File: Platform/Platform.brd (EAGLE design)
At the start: 34 x 34.3 mm, 21 parts, among them IC1 5v

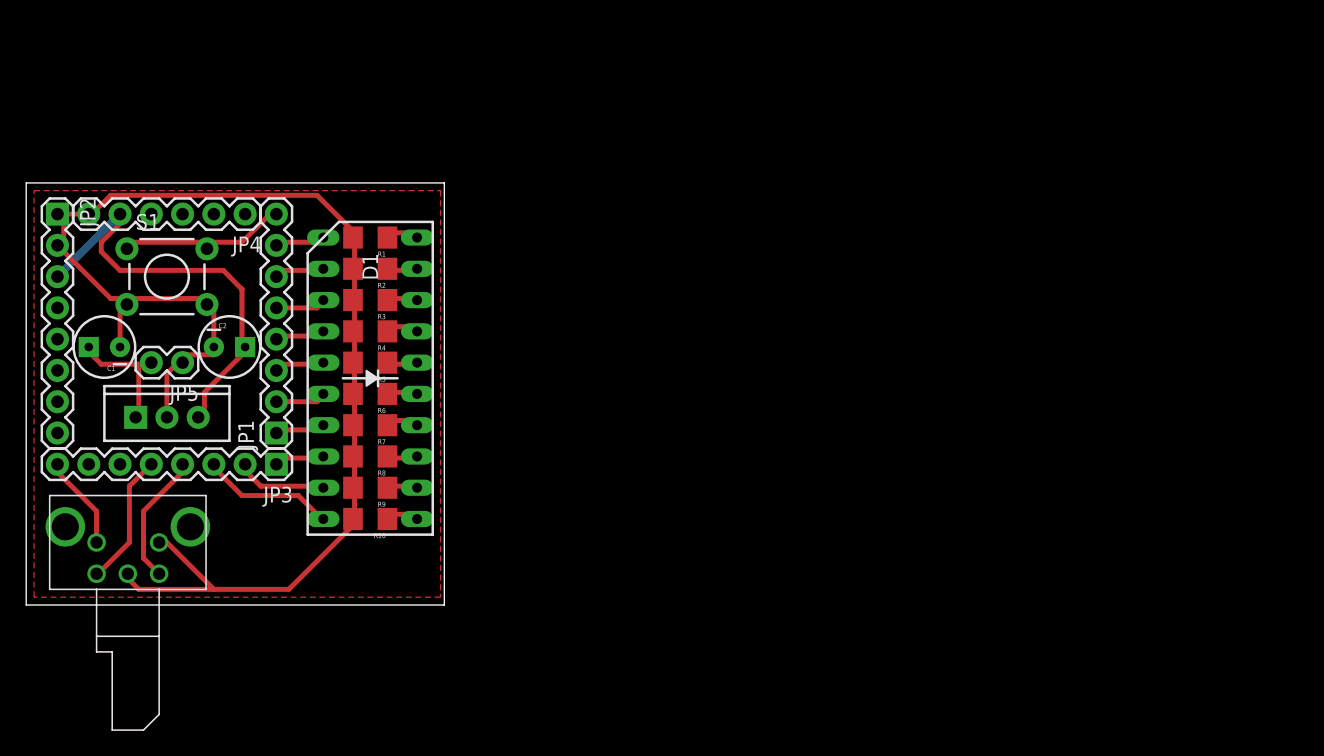
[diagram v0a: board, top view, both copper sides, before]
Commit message: fixed up design rules. Copied the actual newest boards into t the project
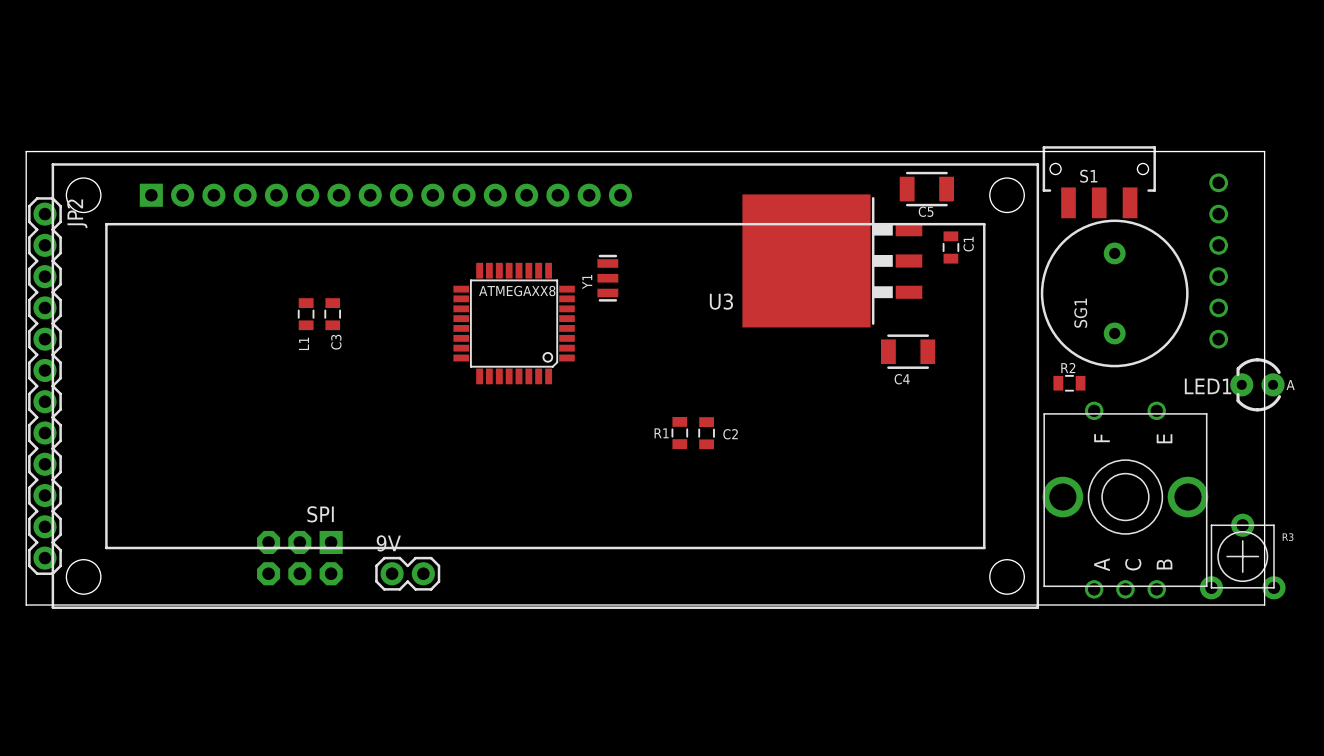
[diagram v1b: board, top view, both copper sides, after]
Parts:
- removed D1: (no value), SparkFun:LED_BARGAPH_10
- removed IC1: 5v, SparkFun:TO220-IGO
- removed JP3: (no value), SparkFun:1X08
- removed JP4: (no value), SparkFun:1X06
- removed JP5: power, SparkFun:1X02
- removed R10, R4, R5, R6, R7, R8, R9: (no value), SparkFun:1206
- removed U$1: EN12-VS11AF, Dustin:12MM_ROTARY
- added 9V: (no value), SparkFun:1X02
- added ATMEGAXX8: ATMEGA168, SparkFun:TQFP32-08
- added C3: 0.1uF, SparkFun:0805
- added C4, C5: 22uf, SparkFun:1210
- added L1: 10uH, SparkFun:0805
- added LED1: (no value), SparkFun:LED3MM
- added SG1: BUZZERPTH, SparkFun:BUZZER-12MM
- added SPI: AVR_SPI_PRG_6NS, SparkFun:2X3-NS
- added U$2: EN12-VS11AFTOPKNOB, Dustin:12MM_ROTATY_TOP
- added U1: LCD-16X2SILK, SparkFun:LCD-16X2
- added U3: IFX25001TC, Dustin:TO263-3
- added Y1: RESONATORSMD, SparkFun:RESONATOR-SMD
- C1, C2: value 22uf -> 0.1uF; device SparkFun:CPOL-RADIAL-10UF-25V -> SparkFun:0805
- JP1: value (none) -> FTDI Basic; device SparkFun:1X08 -> SparkFun:1X06
- JP2: value (none) -> M12PTH; device SparkFun:1X08 -> SparkFun:1X12
- R1: value (none) -> 10K; device SparkFun:1206 -> SparkFun:0805
- R2: value (none) -> 220; device SparkFun:1206 -> SparkFun:0805
- R3: value (none) -> 10k; device SparkFun:1206 -> SparkFun:TRIM_POT_PTH
- S1: value Reset -> (none); device SparkFun:TACTILE-PTH -> SparkFun:SWITCH-SPDT-SMD
- moved JP1 79.2 mm to (96.9, 34.3), turned to 270 degrees
- moved S1 76.2 mm to (87.2, 35.4)
- moved R3 73.9 mm to (98.8, 3.94), turned to 0 degrees
- moved C1 69.2 mm to (75.1, 29.0), turned to 90 degrees
- moved R2 57.6 mm to (84.7, 18.0), turned to 0 degrees
- moved C2 39.4 mm to (55.3, 14.0), turned to 90 degrees
- moved R1 29.7 mm to (53.1, 14.0), turned to 270 degrees
- moved JP2 1.02 mm to (1.52, 31.8)
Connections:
- removed net D11: D1.3, JP1.5
- removed net D12: D1.2, JP1.6
- removed net D13: D1.1, JP1.7
- removed net N$10: D1.20, R1.1
- removed net N$11: D1.19, R2.1
- removed net N$12: D1.18, R3.1
- removed net N$13: D1.17, R4.1
- removed net N$14: D1.16, R5.1
- removed net N$15: D1.15, R6.1
- removed net N$16: D1.14, R7.1
- removed net N$17: D1.13, R8.1
- removed net N$18: D1.12, R9.1
- removed net N$19: D1.11, R10.1
- removed net RST: JP1.8, S1.1, S1.2
- new net AVCC: ATMEGAXX8.18, C3.2, L1.1
- new net CONTRAST: R3.2, U1.3
- new net D11/MOSI: ATMEGAXX8.15, SPI.4
- new net D12/MISO: ATMEGAXX8.16, SPI.1, U$2.E
- new net D13/SCK: ATMEGAXX8.17, LED1.A, SPI.3
- new net N$2: LED1.K, R2.2
- new net RAW_IN: 9V.1, S1.2
- new net RESET: ATMEGAXX8.29, C2.2, R1.1, SPI.5
- new net XTAL1: ATMEGAXX8.7, Y1.1
- new net XTAL2: ATMEGAXX8.8, Y1.3
- net A0: now also ATMEGAXX8.23, U$2.A; no longer JP2.4
- net A1: now also ATMEGAXX8.24, JP2.3; no longer JP2.5
- net A2: now also ATMEGAXX8.25, JP2.4; no longer JP2.6
- net A3: now also ATMEGAXX8.26, JP2.5; no longer JP2.7
- net A4: now also ATMEGAXX8.27, JP2.6; no longer JP2.8
- net A5: now also ATMEGAXX8.28, JP2.7; no longer JP3.8, U$1.D
- net A6: now also ATMEGAXX8.19, JP2.8; no longer JP3.7
- net A7: now also ATMEGAXX8.22, JP2.9; no longer JP3.6
- net AREF: now also ATMEGAXX8.20; no longer JP4.1
- net D10: now also ATMEGAXX8.14, U1.4; no longer D1.4, JP1.4
- net D2: now also ATMEGAXX8.32, U$2.B; no longer JP3.5, U$1.A
- net D3: now also ATMEGAXX8.1, JP2.12; no longer JP3.4, U$1.B
- net D4: now also ATMEGAXX8.2, U1.14; no longer D1.10, JP3.3
- net D5: now also ATMEGAXX8.9, SG1.-; no longer D1.9, JP3.2
- net D6: now also ATMEGAXX8.10, U1.13; no longer D1.8, JP3.1
- net D7: now also ATMEGAXX8.11, U1.12; no longer D1.7, JP1.1
- net D8: now also ATMEGAXX8.12, U1.11; no longer D1.6, JP1.2
- net D9: now also ATMEGAXX8.13, U1.6; no longer D1.5, JP1.3
- net DTR: now also C2.1, JP1.6; no longer JP4.2
- net GND: now also 9V.2, ATMEGAXX8.21, ATMEGAXX8.3, ATMEGAXX8.5, C1.1, C3.1, C4.2, C5.2, JP1.1, JP1.2, R2.1, R3.3, SG1.+, SPI.6, U$2.C, U$2.D, U1.1, U1.16, U1.5, U3.2, U3.TAB, Y1.2; no longer C1.2, C2.2, IC1.GND, JP2.2, JP4.6, JP5.1, R1.2, R10.2, R2.2, R3.2, R4.2, R5.2, R6.2, R7.2, R8.2, R9.2, S1.3, S1.4, U$1.C, U$1.E
- net RAW: now also C4.1, S1.1, U3.1; no longer C1.1, IC1.IN, JP5.2
- net RX: now also ATMEGAXX8.30, JP1.4, JP2.10; no longer JP4.4
- net TX: now also ATMEGAXX8.31, JP1.5, JP2.11; no longer JP4.3
- net VCC: now also ATMEGAXX8.4, ATMEGAXX8.6, C1.2, C5.1, JP1.3, JP2.2, L1.2, R1.2, R3.1, SPI.2, U1.15, U1.2, U3.3; no longer C2.1, IC1.OUT, JP2.3, JP4.5
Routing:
- net GND: track 111.6 -> 0.00 mm
- net VCC: track 35.7 -> 0.00 mm
- net RST: track 14.0 -> 0.00 mm
- net D4: track 10.8 -> 0.00 mm
- net D2: track 10.8 -> 0.00 mm
- net D3: track 10.7 -> 0.00 mm
- net RAW: track 10.2 -> 0.00 mm
- net A5: track 7.67 -> 0.00 mm
- net D5: track 7.61 -> 0.00 mm
- net D6: track 4.14 -> 0.00 mm
- net D9: track 4.14 -> 0.00 mm
- net D12: track 4.14 -> 0.00 mm
- net D11: track 4.12 -> 0.00 mm
- net D8: track 4.12 -> 0.00 mm
- net D10: track 4.04 -> 0.00 mm
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- removed copper zone on layer 1, net GND
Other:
- board size 34 x 34.3 mm -> 100.6 x 36.8 mm
- board text added: "BLK"
- board text added: "GND"
- board text added: "GRN"
- board text added: "RESET"
- board text added: "RX"
- board text added: "TX"
- board text added: "VCC"

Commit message: added barrel connector and touched up top silk
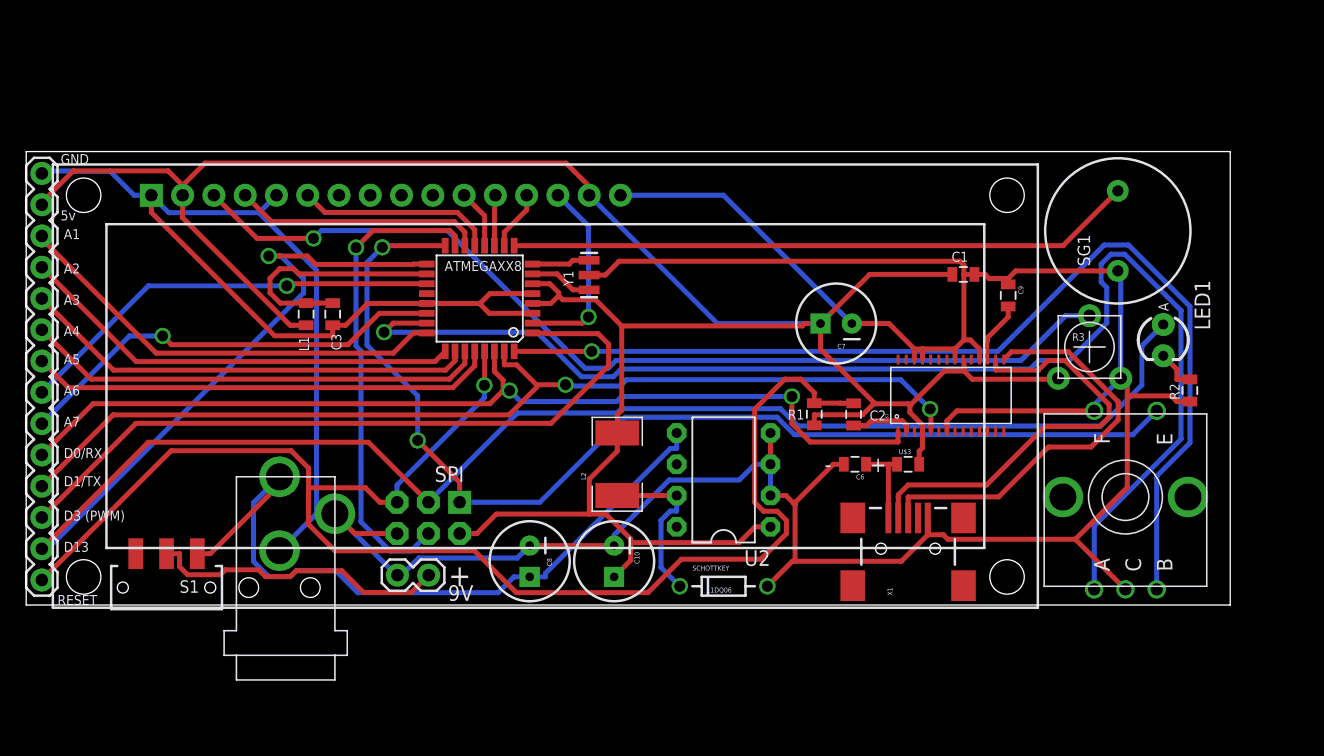
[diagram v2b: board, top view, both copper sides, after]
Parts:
- removed C4, C5: 22uf, SparkFun:1210
- removed JP1: FTDI Basic, SparkFun:1X06
- removed U3: IFX25001TC, Dustin:TO263-3
- added C10: 220uf, SparkFun:CPOL-RADIAL-100UF-25V
- added C6: 0.01uf, Dustin:0805POL
- added C7: 4.7uf, SparkFun:CPOL-RADIAL-100UF-25V
- added C8: 22uf, SparkFun:CPOL-RADIAL-100UF-25V
- added C9: 0.1uf, SparkFun:0805
- added L2: 330uH, SparkFun:INDUCTOR-1206
- added SCHOTTKEY: 11DQ06, SparkFun:DIODE-ZENER
- added U$1: FT232RL, Dustin:TSSOP28
- added U$3: FERRITE, Dustin:0805
- added U$4: DCJACK, Dustin:DCPOWERSOCKETPJ-019
- added U2: LM2574N, Dustin:8DILL
- added X1: USBSMD, SparkFun:USB-MINIB
- JP2: value M12PTH -> M14; device SparkFun:1X12 -> SparkFun:1X14
- moved S1 83.0 mm to (11.4, 1.42), turned to 180 degrees
- moved R3 21.1 mm to (86.4, 21.0)
- moved C2 12.0 mm to (67.2, 15.5)
- moved R1 11.0 mm to (64.0, 15.5)
- moved SPI 10.9 mm to (32.7, 7.08)
- moved R2 9.80 mm to (94.5, 17.4), turned to 90 degrees
- moved LED1 8.46 mm to (92.4, 21.5), turned to 270 degrees
- moved SG1 5.09 mm to (88.7, 30.4)
- moved ATMEGAXX8 3.45 mm to (36.8, 24.9)
- moved JP2 3.31 mm to (1.27, 35.1)
- moved 9V 2.97 mm to (32.7, 2.42), turned to 180 degrees
- moved C1 2.41 mm to (76.1, 26.8), turned to 180 degrees
- moved Y1 1.55 mm to (45.7, 26.8)
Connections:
- new net CTS: U$1.11
- new net N$1: C6.+, U$3.1, X1.VBUS
- new net N$3: L2.P$1, SCHOTTKEY.P$1, U2.7
- new net N$4: U$1.16, X1.D-
- new net N$5: U$1.15, X1.D+
- new net N$6: C9.2, U$1.17
- net D13/SCK: now also JP2.13
- net DTR: now also U$1.2; no longer JP1.6
- net GND: now also C10.2, C6.-, C7.2, C8.2, C9.1, SCHOTTKEY.P$2, U$1.18, U$1.21, U$1.25, U$1.26, U$1.7, U$4.2, U$4.3, U2.2, U2.3, U2.4, X1.GND; no longer C4.2, C5.2, JP1.1, JP1.2, U3.2, U3.TAB
- net RAW: now also C8.1, U$4.1C, U2.5; no longer C4.1, U3.1
- net RESET: now also JP2.14
- net RX: now also U$1.1; no longer JP1.4
- net TX: now also U$1.5; no longer JP1.5
- net VCC: now also C10.1, C7.1, L2.P$2, U$1.20, U$1.4, U$3.2, U2.1; no longer C5.1, JP1.3, U3.3
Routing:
- net GND: track 0.00 -> 329.7 mm
- net VCC: track 0.00 -> 212.0 mm
- net D13/SCK: track 0.00 -> 153.4 mm, vias 0 -> 1
- net RESET: track 0.00 -> 119.3 mm, vias 0 -> 1
- net A0: track 0.00 -> 105.0 mm, vias 0 -> 1
- net D12/MISO: track 0.00 -> 90.4 mm, vias 0 -> 2
- net D2: track 0.00 -> 84.6 mm, vias 0 -> 1
- net TX: track 0.00 -> 83.2 mm, vias 0 -> 2
- net RX: track 0.00 -> 79.4 mm, vias 0 -> 2
- net CONTRAST: track 0.00 -> 79.2 mm, vias 0 -> 1
- net RAW: track 0.00 -> 59.5 mm
- net D3: track 0.00 -> 59.4 mm
- net D5: track 0.00 -> 50.9 mm
- net D11/MOSI: track 0.00 -> 39.1 mm, vias 0 -> 1
- net A5: track 0.00 -> 38.0 mm
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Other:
- board size 100.6 x 36.8 mm -> 97.8 x 36.8 mm
- board text added: "+"
- board text added: "5v"
- board text added: "A1"
- board text added: "A2"
- board text added: "A3"
- board text added: "A4"
- board text added: "A5"
- board text added: "A6"
- board text added: "A7"
- board text added: "D0/RX"
- board text added: "D1/TX"
- board text added: "D13"
- board text added: "D3 (PWM)"
- board text removed: "BLK"
- board text removed: "GRN"
- board text removed: "RX"
- board text removed: "TX"
- board text removed: "VCC"

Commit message: updated component locations and traces
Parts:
- added GOLD_ORB_SM1: OSHWLOGO_GOLD_ORB_SM, NBitWonder:OSHW2
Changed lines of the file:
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@@
 <attribute name="VALUE" x="22.518" y="8.082" size="1.27" layer="27" rot="R180"/>
 </element>
+<element name="GOLD_ORB_SM1" library="NBitWonder" package="OSHW2" value="OSHWLOGO_GOLD_ORB_SM" x="89.916" y="29.464"/>
 </elements>
 <signals>

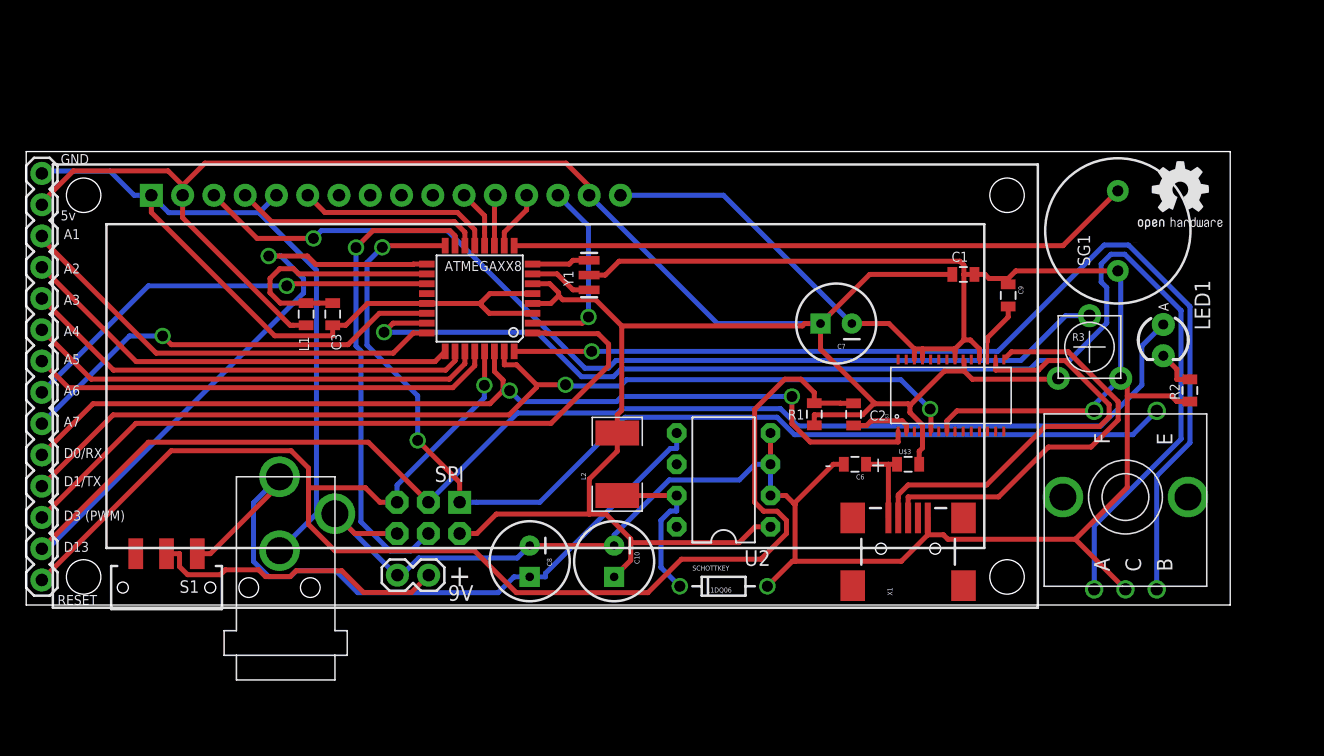
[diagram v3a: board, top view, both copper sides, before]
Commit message: More board tweak, added part list and toner file used to make pre prototype 2
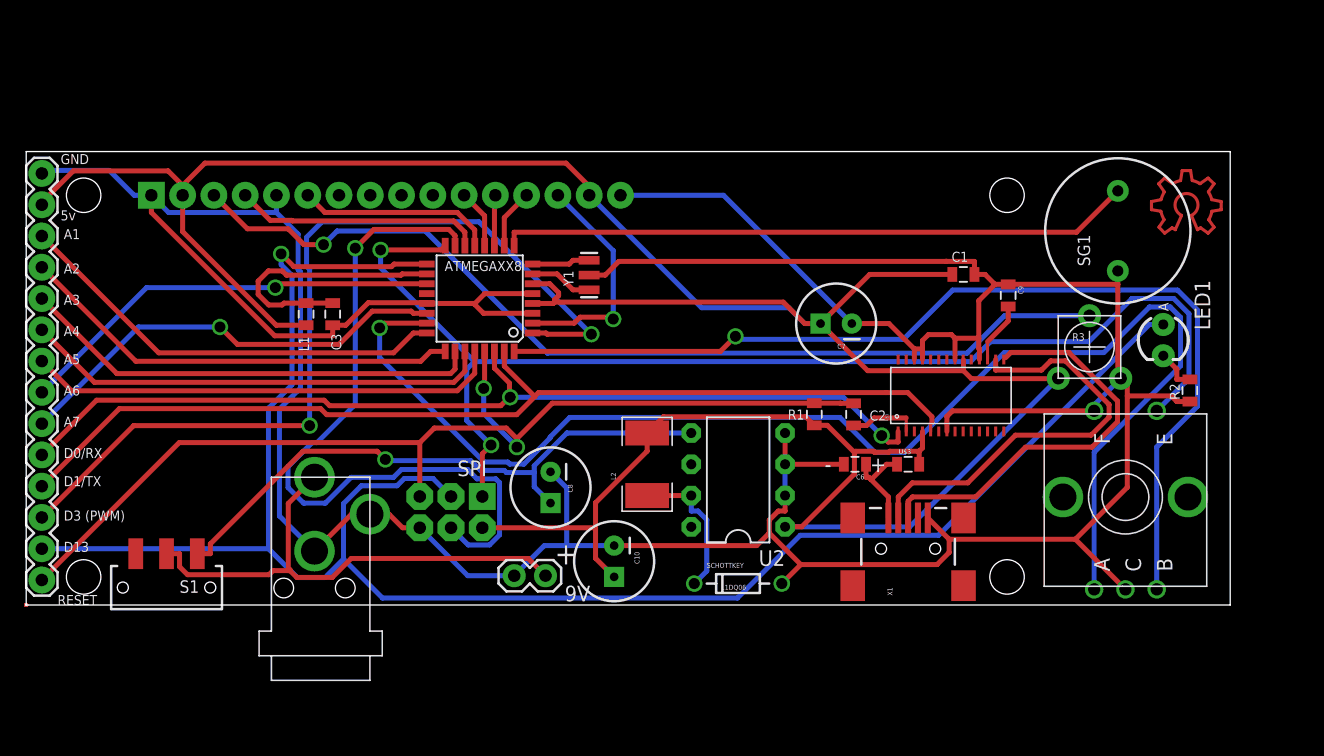
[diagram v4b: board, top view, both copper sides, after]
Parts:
- removed GOLD_ORB_SM1: OSHWLOGO_GOLD_ORB_SM, NBitWonder:OSHW2
- added LOGO1: OSHW_LOGO_10MIL, ohw-logo:OSHW_10X200_NOTEXT_COPPER
- JP2: value M14 -> M14B; device SparkFun:1X14 -> Dustin:1X14B
- U1: value LCD-16X2SILK -> LCD-16X2NOSILK; device SparkFun:LCD-16X2 -> SparkFun:LCD-16X2_NOSILK
- moved 9V 9.49 mm to (42.2, 2.38)
- moved C8 6.23 mm to (42.6, 9.55)
- moved U$4 2.84 mm to (23.4, 10.4)
- moved L2 2.43 mm to (50.4, 11.4)
- moved SPI 1.90 mm to (34.5, 7.54)
- moved SCHOTTKEY 1.19 mm to (57.8, 1.74)
- moved U2 1.18 mm to (57.8, 10.2)
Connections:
- net RAW: no longer U$4.1C
- net RAW_IN: now also U$4.1C
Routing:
- net RESET: track 119.3 -> 86.6 mm, vias 1 -> 2
- net VCC: track 212.0 -> 236.7 mm
- net D11/MOSI: track 39.1 -> 60.1 mm
- net RAW_IN: track 24.5 -> 42.3 mm
- net D3: track 59.4 -> 72.5 mm, vias 0 -> 2
- net RAW: track 59.5 -> 49.4 mm, vias 0 -> 1
- net D12/MISO: track 90.4 -> 99.6 mm
- net D4: track 15.7 -> 18.7 mm
- net A0: track 105.0 -> 108.1 mm
- net N$7: track 0.00 -> 2.27 mm
- net D2: track 84.6 -> 82.5 mm
- net GND: track 329.7 -> 331.7 mm
- net AVCC: track 19.8 -> 21.8 mm
- net D13/SCK: track 153.4 -> 155.3 mm
- net N$3: track 13.7 -> 12.0 mm
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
